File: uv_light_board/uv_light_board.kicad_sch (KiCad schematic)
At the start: 14 parts, among them J1 Power, J2 Power

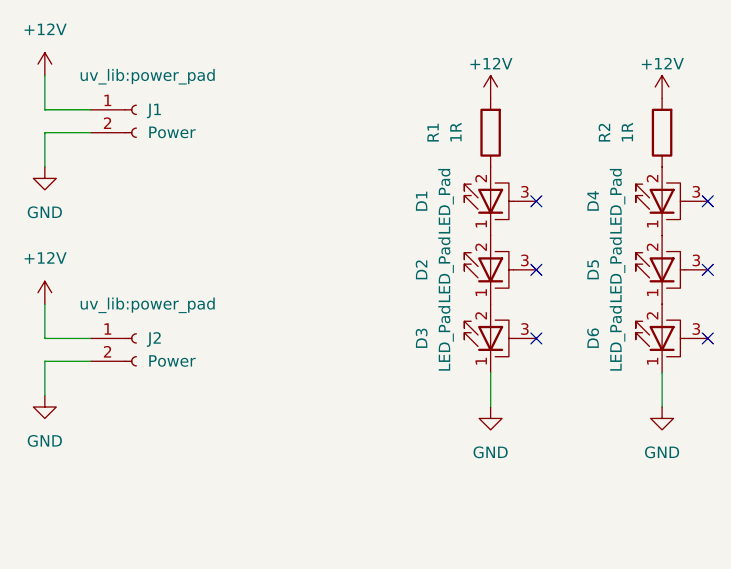
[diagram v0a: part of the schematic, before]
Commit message: Replacing the UV led with an SMD LED we can buy PnP
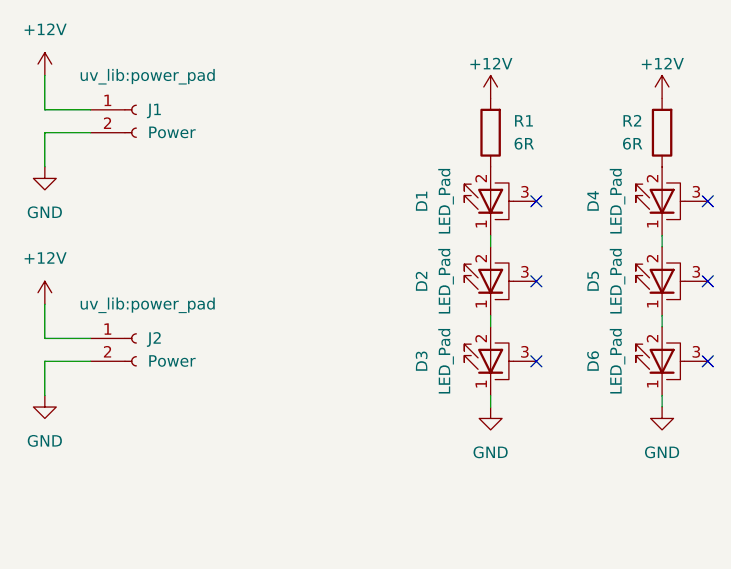
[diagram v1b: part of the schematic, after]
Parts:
- D1, D2, D3, D4, D5, D6: footprint LED_SMD:LED_1W_3W_R8 -> uv_lib:SMD3535-3P
- R1, R2: value 1R -> 6R

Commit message: Adding part numbers to schematic
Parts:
- D1, D2, D3, D4, D5, D6: JLCPCB Part (none) -> C2833503
- R1, R2: JLCPCB Part (none) -> C3000793
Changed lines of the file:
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@@
+			)
+		)
+		(property "JLCPCB Part" "C2833503"
+			(at 160.02 86.36 0)
+			(effects
+				(font
+					(size 1.27 1.27)
+				)
+				(hide yes)
 			)
 		)
@@
 			)
 		)
+		(property "JLCPCB Part" "C2833503"
+			(at 160.02 95.25 0)
+			(effects
+				(font
+					(size 1.27 1.27)
+				)
+				(hide yes)
+			)
+		)
 		(pin "1"
 		)
@@
 			)
 		)
+		(property "JLCPCB Part" "C3000793"
+			(at 179.07 69.85 0)
+			(effects
+				(font
+					(size 1.27 1.27)
+				)
+				(hide yes)
+			)
+		)
 		(pin "1"
 		)
@@
 			)
 		)
+		(property "JLCPCB Part" "C2833503"
+			(at 179.07 95.25 0)
+			(effects
+				(font
+					(size 1.27 1.27)
+				)
+				(hide yes)
+			)
+		)
 		(pin "1"
 		)
@@
 			)
 		)
+		(property "JLCPCB Part" "C2833503"
+			(at 179.07 77.47 0)
+			(effects
+				(font
+					(size 1.27 1.27)
+				)
+				(hide yes)
+			)
+		)
 		(pin "1"
 		)
@@
 			)
 		)
+		(property "JLCPCB Part" "C2833503"
+			(at 160.02 77.47 0)
+			(effects
+				(font
+					(size 1.27 1.27)
+				)
+				(hide yes)
+			)
+		)
 		(pin "1"
 		)
@@
 			)
 		)
+		(property "JLCPCB Part" "C2833503"
+			(at 179.07 86.36 0)
+			(effects
+				(font
+					(size 1.27 1.27)
+				)
+				(hide yes)
+			)
+		)
 		(pin "1"
 		)
@@
 			)
 		)
+		(property "JLCPCB Part" "C3000793"
+			(at 160.02 69.85 0)
+			(effects
+				(font
+					(size 1.27 1.27)
+				)
+				(hide yes)
+			)
+		)

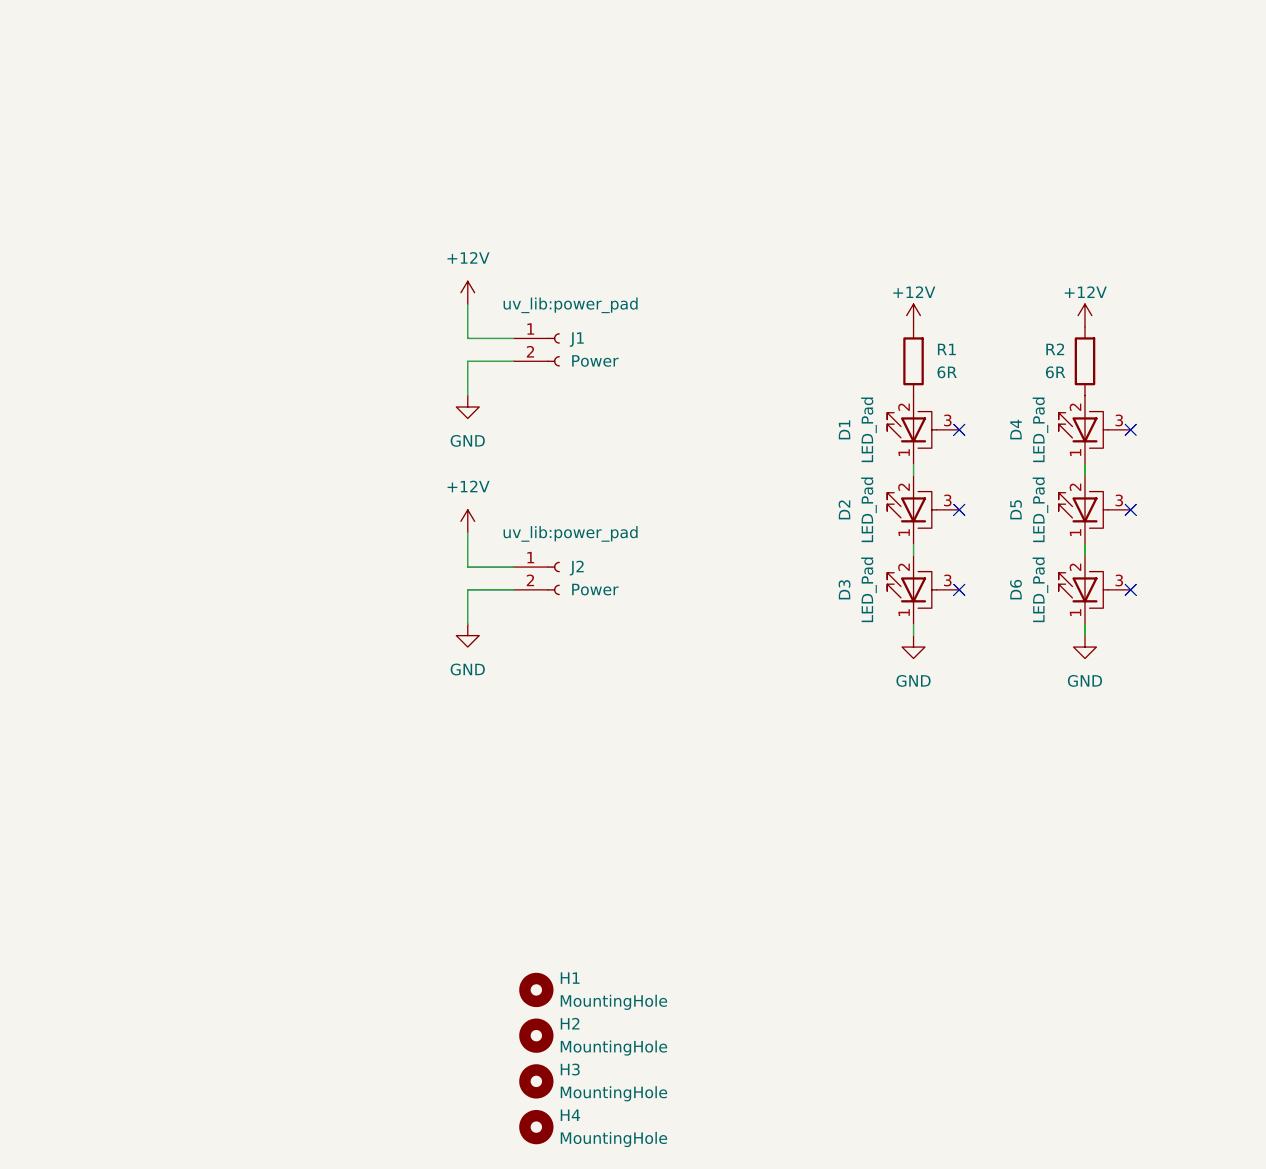
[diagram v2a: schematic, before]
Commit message: Adding more resistor choices to light PCB, tweaking LED footprint
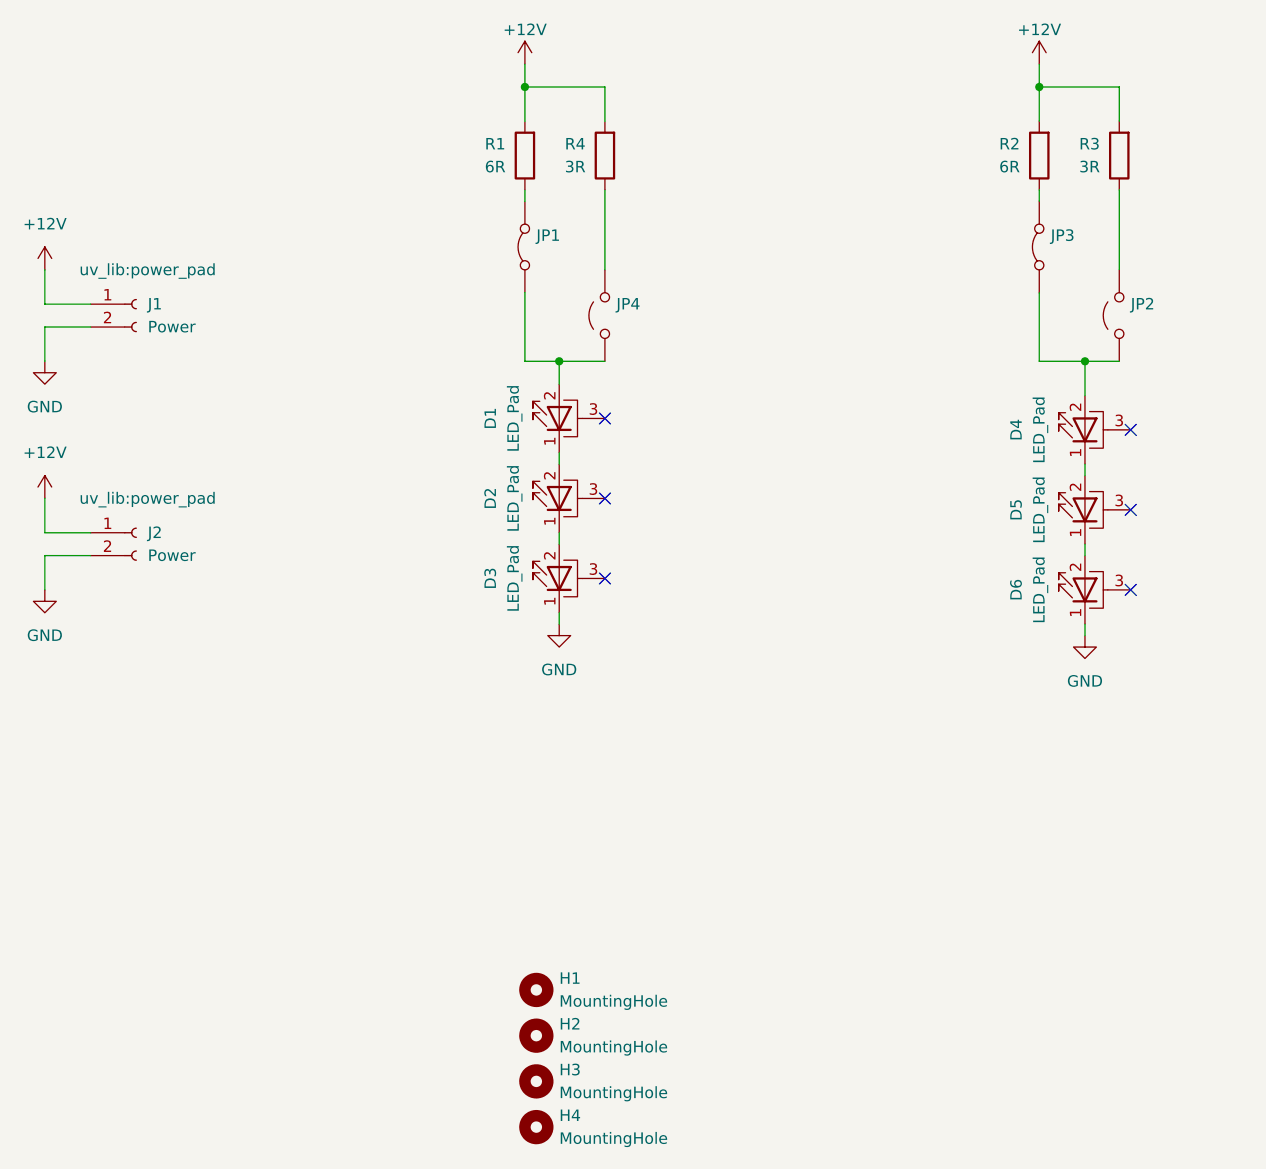
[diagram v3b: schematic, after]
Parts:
- added JP1, JP3: Jumper_2_Bridged, Jumper:SolderJumper-2_P1.3mm_Bridged2Bar_Pad1.0x1.5mm, symbol Jumper:Jumper_2_Bridged
- added JP2, JP4: Jumper_2_Open, Jumper:SolderJumper-2_P1.3mm_Open_Pad1.0x1.5mm, symbol Jumper:Jumper_2_Open
- added R3, R4: 3R, Resistor_SMD:R_2512_6332Metric, symbol Device:R
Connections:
- net +12V: now also R3.2, R4.2
- net at R2.1: now also JP3.2 (B); no longer D4.2 (A)
- net at R1.1: now also JP1.2 (B); no longer D1.2 (A)
- new net: D1.2 (A), JP1.1 (A), JP4.1 (A)
- new net: JP4.2 (B), R4.1
- new net: D4.2 (A), JP2.1 (A), JP3.1 (A)
- new net: JP2.2 (B), R3.1
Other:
- moved on the sheet: D1, D2, D3, J1, J2, R2

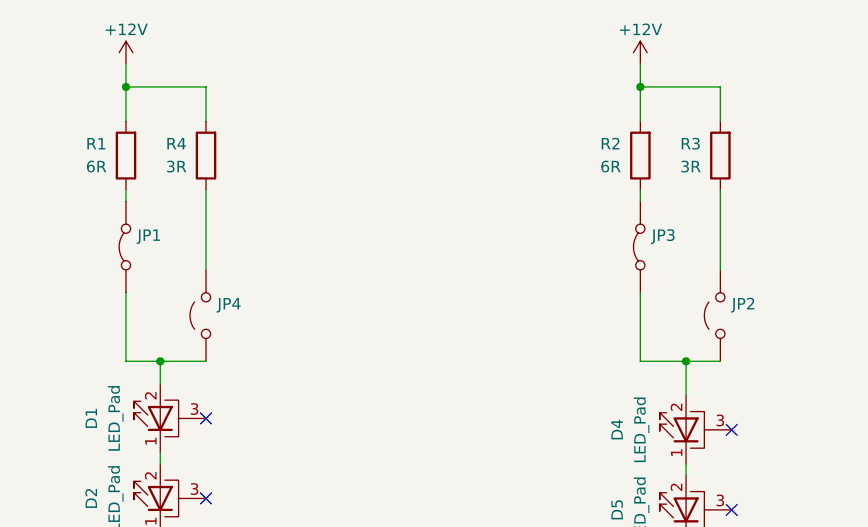
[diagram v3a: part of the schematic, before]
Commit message: Adding 3rd tuning resistor, fixing footprints on PCB
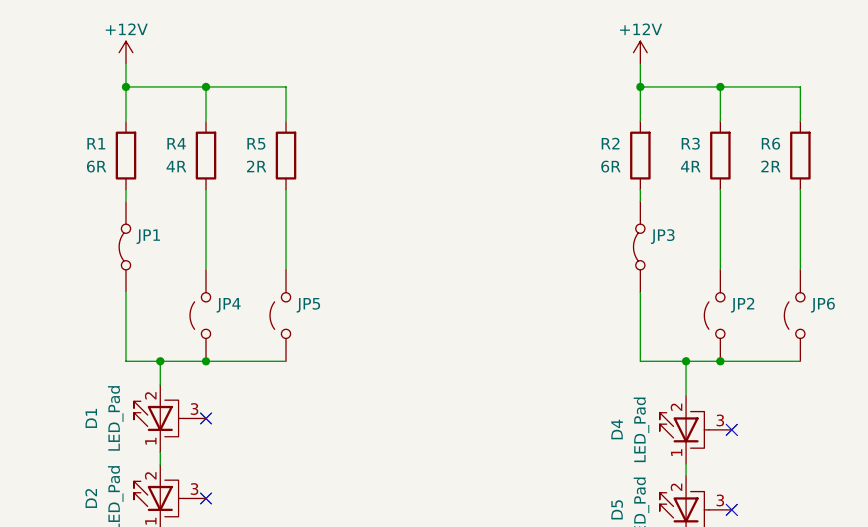
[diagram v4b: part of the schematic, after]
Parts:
- added JP5, JP6: Jumper_2_Open, Jumper:SolderJumper-2_P1.3mm_Open_Pad1.0x1.5mm, symbol Jumper:Jumper_2_Open
- added R5, R6: 2R, Resistor_SMD:R_2512_6332Metric, symbol Device:R
- R1, R2: JLCPCB Part C3000793 -> C2765522
- R3, R4: value 3R -> 4R; JLCPCB Part C15120 -> C39356
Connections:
- net +12V: now also R5.2, R6.2
- net at D1.2 (A), JP1.1 (A), JP4.1 (A): now also JP5.1 (A)
- net at D4.2 (A), JP2.1 (A), JP3.1 (A): now also JP6.1 (A)
- new net: JP5.2 (B), R5.1
- new net: JP6.2 (B), R6.1
